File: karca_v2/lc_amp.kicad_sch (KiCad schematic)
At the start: 19 parts, among them U18 AD8223, U6 TLV9304xD, U7 TLV9304xD

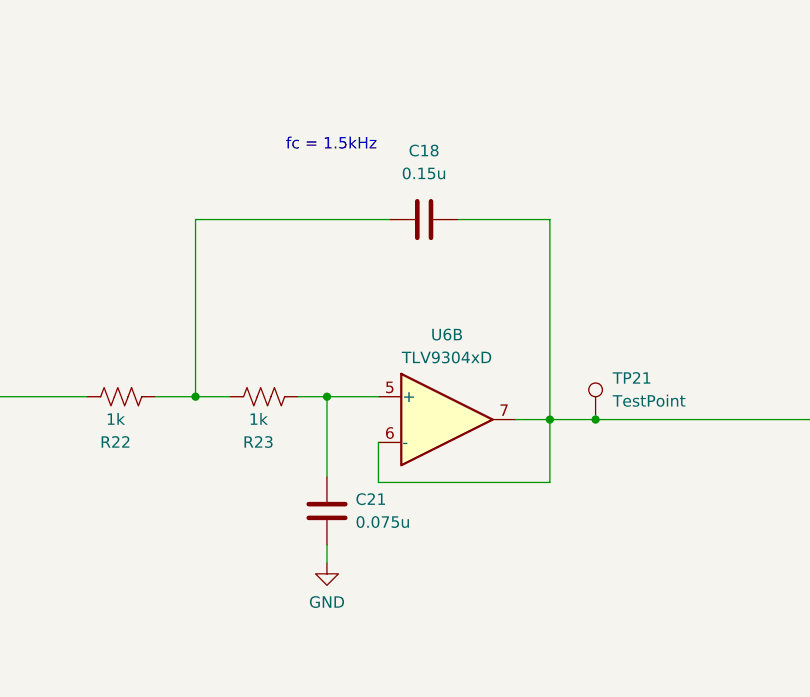
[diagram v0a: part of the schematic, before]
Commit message: changed capacitor values and sizes for production
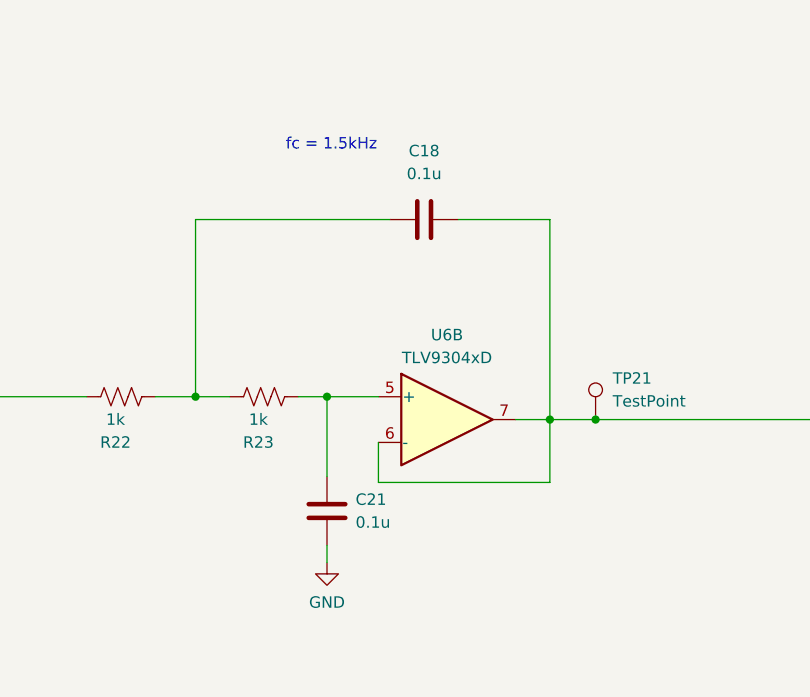
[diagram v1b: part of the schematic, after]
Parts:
- C18: value 0.15u -> 0.1u
- C21: value 0.075u -> 0.1u
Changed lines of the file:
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@@
       (effects (font (size 1.27 1.27)))
     )
-    (property "Value" "0.15u" (at 191.135 50.165 90)
+    (property "Value" "0.1u" (at 191.135 50.165 90)
       (effects (font (size 1.27 1.27)))
     )
@@
       (effects (font (size 1.27 1.27)) (justify right))
     )
-    (property "Value" "0.075u" (at 183.515 88.9 0)
-      (effects (font (size 1.27 1.27)) (justify right))
-    )
+    (property "Value" "0.1u" (at 183.515 88.9 0)
+      (effects (font (size 1.27 1.27)) (justify right))
+    )

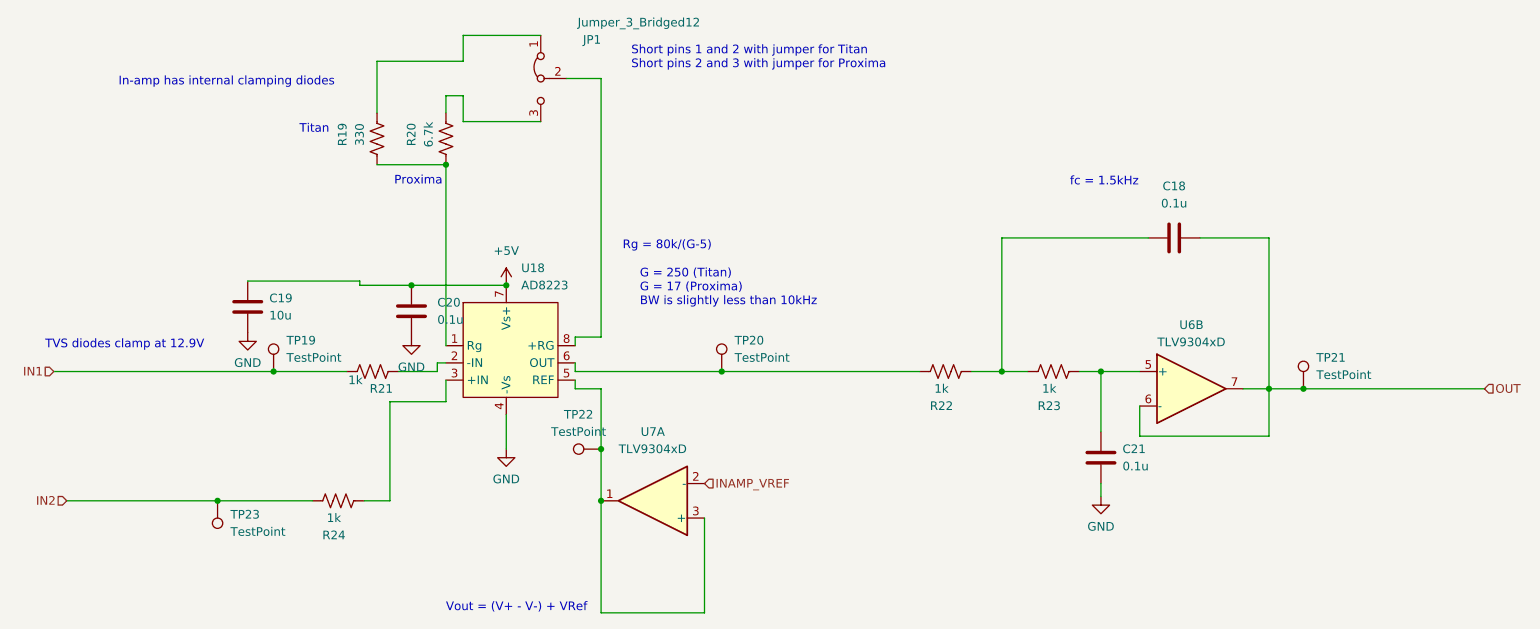
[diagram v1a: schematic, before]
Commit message: cleaned up documentation. Added production files and BOM. Marked Thermocouple components and THT components as DNP (excluded them from BOM too) to match version sent to JLCPCB for fabrication
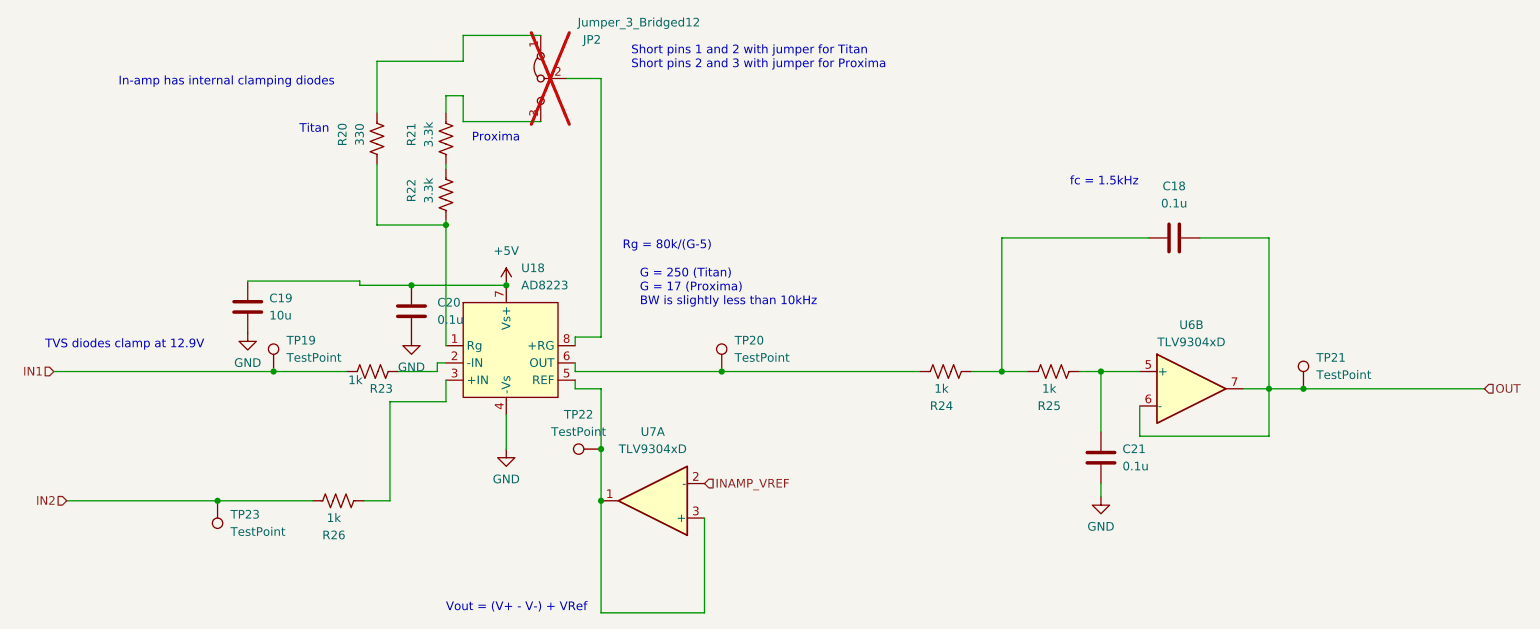
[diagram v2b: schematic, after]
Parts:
- added R22: 3.3k, Resistor_SMD:R_0402_1005Metric, symbol Device:R_US
- JP2: renamed from JP1; now not fitted; now left out of the parts list
- R21: renamed from R20; value 6.7k -> 3.3k; footprint Resistor_SMD:R_1206_3216Metric -> Resistor_SMD:R_0402_1005Metric
- renumbered R19 to R20, R21 to R23, R22 to R24, R23 to R25, R24 to R26
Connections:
- net at R20.1, U18.1 (Rg): now also R22.1; no longer R21.1
- new net: R21.1, R22.2
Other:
- company: (none) -> Rice Eclipse
- title: (none) -> kARCA 2.0 Engine Control System

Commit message: new design: chip on board
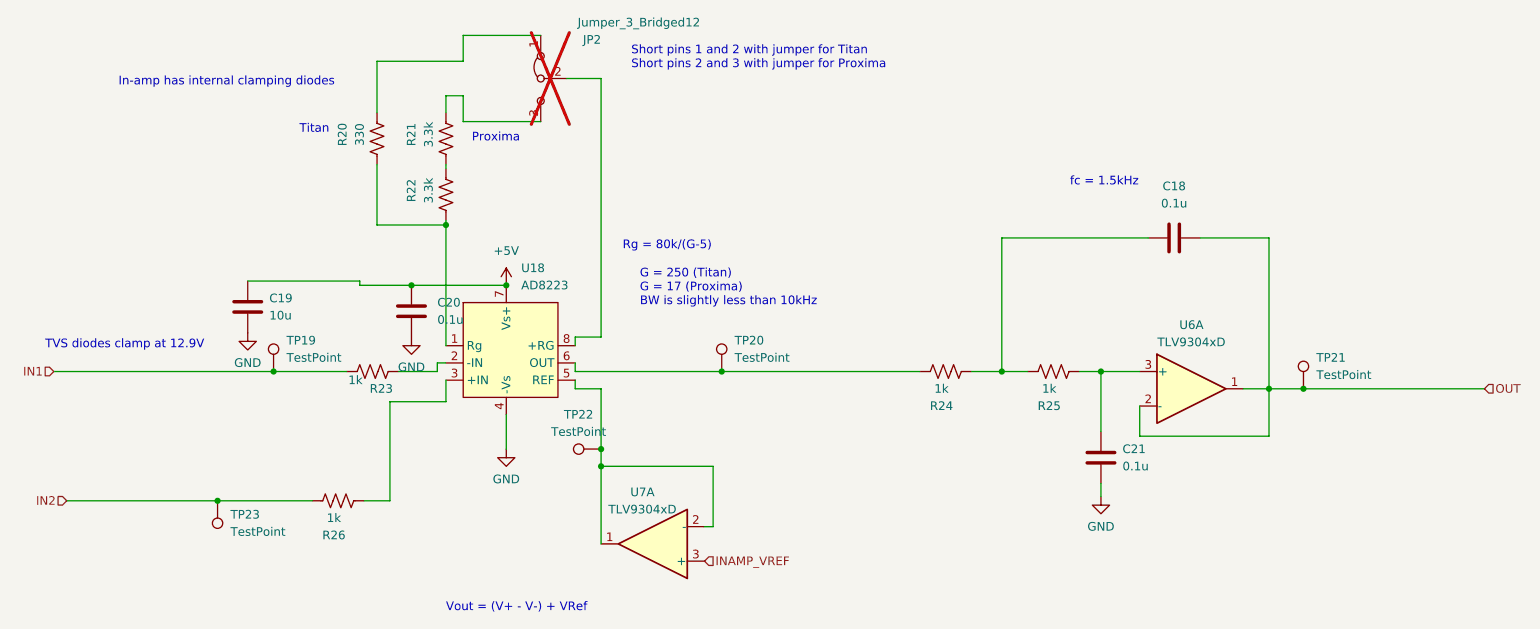
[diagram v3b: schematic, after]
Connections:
- net INAMP_VREF: now also U7.3 (+); no longer U7.2 (-)
- net OUT: now also U6.1, U6.2 (-); no longer U6.6 (-), U6.7
- net at TP22.1, U18.5 (REF), U7.1: now also U7.2 (-); no longer U7.3 (+)
- net at C21.2, R25.1: now also U6.3 (+); no longer U6.5 (+)
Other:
- moved on the sheet: U7A
